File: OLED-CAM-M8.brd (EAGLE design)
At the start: 87.6 x 61 mm, 16 parts, among them J5 U.FL

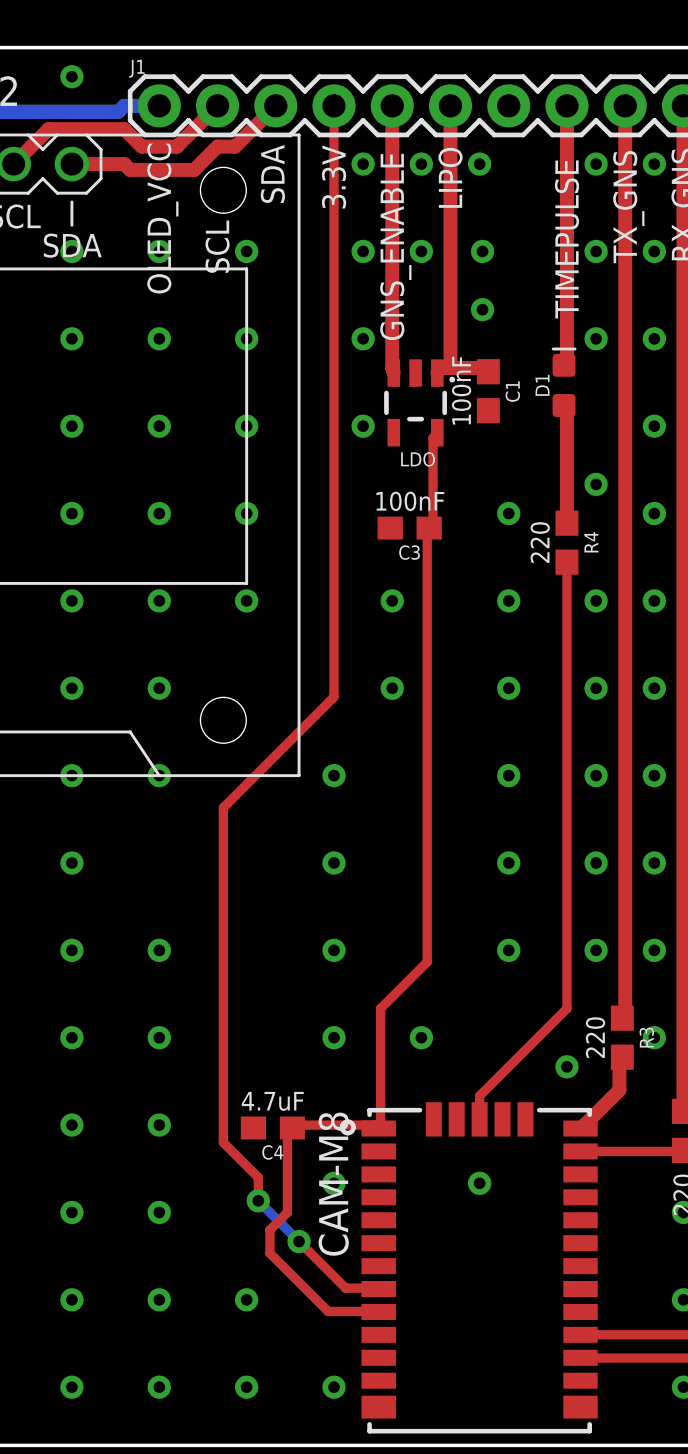
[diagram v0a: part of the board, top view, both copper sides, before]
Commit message: Moved 3v rail
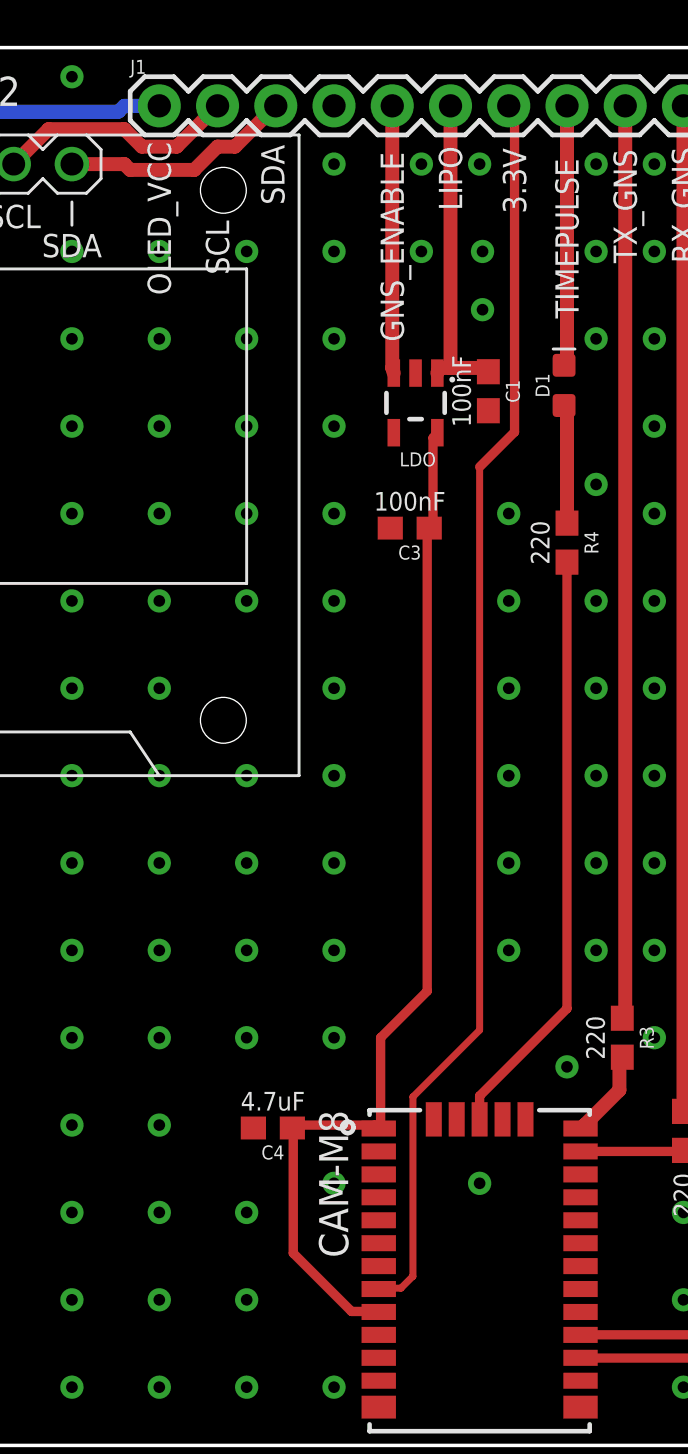
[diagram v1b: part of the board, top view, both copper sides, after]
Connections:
- net 3.3V: now also J1.7; no longer J1.4
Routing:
- net 3.3V: track 57.2 -> 54.7 mm, vias 2 -> 0
- net GNS_VCC: track 47.3 -> 45.6 mm
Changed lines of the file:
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@@
 Only one ANT jumper
 should be bridged</text>
-<wire x1="42.037" y1="14.859" x2="42.037" y2="13.589" width="0.0508" layer="41"/>
 <text x="58.928" y="54.102" size="1.016" layer="25" font="vector" ratio="20" rot="R90">GND</text>
 <text x="56.388" y="52.451" size="1.016" layer="25" font="vector" ratio="20" rot="R90">SPARE</text>
@@
 <text x="43.688" y="53.848" size="1.016" layer="25" font="vector" ratio="20" rot="R90">LIPO</text>
 <text x="41.148" y="48.133" size="1.016" layer="25" font="vector" ratio="20" rot="R90">GNS_ENABLE</text>
-<text x="38.608" y="53.848" size="1.016" layer="25" font="vector" ratio="20" rot="R90">3.3V</text>
+<text x="46.482" y="53.721" size="1.016" layer="25" font="vector" ratio="20" rot="R90">3.3V</text>
 <text x="35.941" y="54.102" size="1.016" layer="25" font="vector" ratio="20" rot="R90">SDA</text>
 <text x="30.988" y="50.165" size="1.016" layer="25" font="vector" ratio="20" rot="R90">OLED_VCC</text>
@@
 <clearance class="1" value="0.4064"/>
 </class>
-<class number="2" name="gns" width="0.4064" drill="0">
-<clearance class="2" value="0.4064"/>
+<class number="2" name="gns" width="0.3048" drill="0">
+<clearance class="2" value="0.3048"/>
 </class>
 </classes>
@@
 <via x="44.577" y="52.07" extent="1-16" drill="0.508"/>
 <via x="41.91" y="52.07" extent="1-16" drill="0.508"/>
-<via x="39.37" y="48.26" extent="1-16" drill="0.508"/>
-<via x="39.37" y="52.07" extent="1-16" drill="0.508"/>
-<via x="39.37" y="44.45" extent="1-16" drill="0.508"/>
-<via x="39.37" y="55.88" extent="1-16" drill="0.508"/>
 <via x="57.15" y="40.64" extent="1-16" drill="0.508"/>
 <via x="57.15" y="44.45" extent="1-16" drill="0.508"/>
@@
 <via x="64.77" y="13.97" extent="1-16" drill="0.508"/>
 <via x="38.1" y="17.78" extent="1-16" drill="0.508"/>
-<via x="41.91" y="17.78" extent="1-16" drill="0.508"/>
-<via x="40.64" y="33.02" extent="1-16" drill="0.508"/>
-<via x="40.64" y="36.83" extent="1-16" drill="0.508"/>
 <via x="45.72" y="40.64" extent="1-16" drill="0.508"/>
+<via x="34.29" y="17.78" extent="1-16" drill="0.508"/>
+<via x="34.29" y="10.16" extent="1-16" drill="0.508"/>
+<via x="34.29" y="21.59" extent="1-16" drill="0.508"/>
+<via x="34.29" y="25.4" extent="1-16" drill="0.508"/>
+<via x="30.48" y="25.4" extent="1-16" drill="0.508"/>
+<via x="34.29" y="29.21" extent="1-16" drill="0.508"/>
+<via x="38.1" y="33.02" extent="1-16" drill="0.508"/>
+<via x="38.1" y="36.83" extent="1-16" drill="0.508"/>
+<via x="38.1" y="40.64" extent="1-16" drill="0.508"/>
+<via x="38.1" y="44.45" extent="1-16" drill="0.508"/>
+<via x="38.1" y="48.26" extent="1-16" drill="0.508"/>
+<via x="38.1" y="52.07" extent="1-16" drill="0.508"/>
+<via x="38.1" y="55.88" extent="1-16" drill="0.508"/>
 </signal>
 <signal name="3.3V" class="2">
 <contactref element="U$5" pad="8"/>
-<contactref element="J1" pad="4"/>
-<wire x1="38.608" y1="6.858" x2="39.878" y2="6.858" width="0.4064" layer="1"/>
-<wire x1="36.576" y1="8.89" x2="38.608" y2="6.858" width="0.4064" layer="1"/>
-<wire x1="34.798" y1="10.668" x2="36.576" y2="8.89" width="0.4064" layer="16"/>
-<wire x1="34.798" y1="11.684" x2="34.798" y2="10.668" width="0.4064" layer="1"/>
-<wire x1="33.274" y1="13.208" x2="34.798" y2="11.684" width="0.4064" layer="1"/>
-<wire x1="33.274" y1="27.813" x2="33.274" y2="13.208" width="0.4064" layer="1"/>
-<wire x1="38.1" y1="32.639" x2="33.274" y2="27.813" width="0.4064" layer="1"/>
-<wire x1="38.1" y1="58.42" x2="38.1" y2="32.639" width="0.4064" layer="1"/>
-<wire x1="39.878" y1="6.858" x2="40.05" y2="6.82" width="0.4064" layer="1"/>
-<via x="36.576" y="8.89" extent="1-16" drill="0.508"/>
-<via x="34.798" y="10.668" extent="1-16" drill="0.508"/>
+<contactref element="J1" pad="7"/>
+<wire x1="45.974" y1="44.196" x2="44.45" y2="42.672" width="0.4064" layer="1"/>
+<wire x1="45.974" y1="58.166" x2="45.974" y2="44.196" width="0.4064" layer="1"/>
+<wire x1="45.72" y1="58.42" x2="45.974" y2="58.166" width="0.4064" layer="1"/>
+<wire x1="44.45" y1="18.1102625" x2="44.45" y2="42.672" width="0.3048" layer="1"/>
+<wire x1="44.45" y1="18.1102625" x2="41.5412" y2="15.2014625" width="0.3048" layer="1"/>
+<wire x1="41.5412" y1="7.366" x2="41.5412" y2="15.2014625" width="0.3048" layer="1"/>
+<wire x1="41.021" y1="6.858" x2="40.132" y2="6.858" width="0.3048" layer="1"/>
+<wire x1="41.529" y1="7.366" x2="41.021" y2="6.858" width="0.3048" layer="1"/>
+<wire x1="41.529" y1="7.366" x2="41.5412" y2="7.366" width="0.3048" layer="1"/>
+<wire x1="40.132" y1="6.858" x2="40.05" y2="6.82" width="0.3048" layer="1"/>
 </signal>
 <signal name="TX_GNS">
@@
 <contactref element="U$5" pad="9"/>
 <contactref element="U$5" pad="1"/>
-<wire x1="42.164" y1="40.005" x2="42.252" y2="40.005" width="0.4064" layer="1"/>
-<wire x1="42.418" y1="40.005" x2="42.252" y2="40.005" width="0.4064" layer="1"/>
-<wire x1="37.846" y1="5.842" x2="39.878" y2="5.842" width="0.4064" layer="1"/>
-<wire x1="35.306" y1="8.382" x2="37.846" y2="5.842" width="0.4064" layer="1"/>
-<wire x1="35.306" y1="9.398" x2="35.306" y2="8.382" width="0.4064" layer="1"/>
-<wire x1="36.068" y1="10.16" x2="35.306" y2="9.398" width="0.4064" layer="1"/>
-<wire x1="36.068" y1="13.716" x2="36.068" y2="10.16" width="0.4064" layer="1"/>
-<wire x1="39.878" y1="5.842" x2="40.05" y2="5.82" width="0.4064" layer="1"/>
-<wire x1="36.068" y1="13.716" x2="36.283" y2="13.843" width="0.4064" layer="1"/>
 <wire x1="36.322" y1="13.97" x2="39.878" y2="13.97" width="0.4064" layer="1"/>
 <wire x1="39.878" y1="13.97" x2="40.05" y2="13.82" width="0.4064" layer="1"/>
 <wire x1="36.322" y1="13.97" x2="36.283" y2="13.843" width="0.4064" layer="1"/>
 <wire x1="42.418" y1="43.942" x2="42.418" y2="40.132" width="0.4064" layer="1"/>
-<wire x1="42.418" y1="40.132" x2="42.252" y2="40.005" width="0.4064" layer="1"/>
 <wire x1="42.418" y1="43.942" x2="42.606" y2="44.1659" width="0.4064" layer="1"/>
-<wire x1="42.164" y1="21.082" x2="42.164" y2="39.878" width="0.4064" layer="1"/>
-<wire x1="40.132" y1="19.05" x2="42.164" y2="21.082" width="0.4064" layer="1"/>
-<wire x1="40.132" y1="13.97" x2="40.132" y2="19.05" width="0.4064" layer="1"/>
-<wire x1="42.164" y1="39.878" x2="42.252" y2="40.005" width="0.4064" layer="1"/>
+<wire x1="38.862" y1="5.842" x2="39.878" y2="5.842" width="0.4064" layer="1"/>
+<wire x1="36.322" y1="8.382" x2="38.862" y2="5.842" width="0.4064" layer="1"/>
+<wire x1="36.322" y1="13.716" x2="36.322" y2="8.382" width="0.4064" layer="1"/>
+<wire x1="39.878" y1="5.842" x2="40.05" y2="5.82" width="0.4064" layer="1"/>
+<wire x1="42.164" y1="19.812" x2="42.164" y2="39.878" width="0.4064" layer="1"/>
+<wire x1="40.132" y1="17.78" x2="42.164" y2="19.812" width="0.4064" layer="1"/>
+<wire x1="40.132" y1="13.97" x2="40.132" y2="17.78" width="0.4064" layer="1"/>
 <wire x1="40.132" y1="13.97" x2="40.05" y2="13.82" width="0.4064" layer="1"/>
+<wire x1="42.418" y1="40.132" x2="42.252" y2="40.005" width="0.3048" layer="1"/>
+<wire x1="42.164" y1="39.878" x2="42.252" y2="40.005" width="0.3048" layer="1"/>
+<wire x1="36.322" y1="13.716" x2="36.283" y2="13.843" width="0.3048" layer="1"/>
 </signal>
 <signal name="GNS_ENABLE">

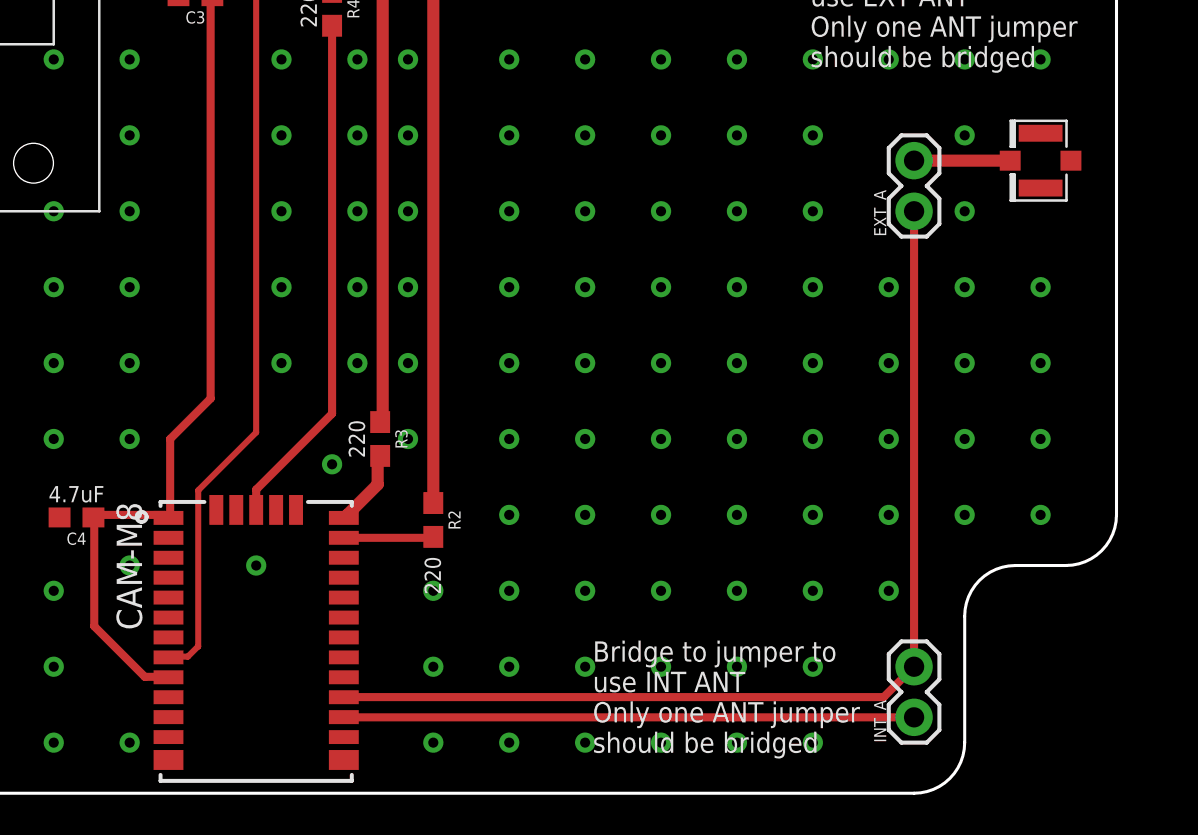
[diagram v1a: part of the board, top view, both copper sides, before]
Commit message: removed ufl and jumpers
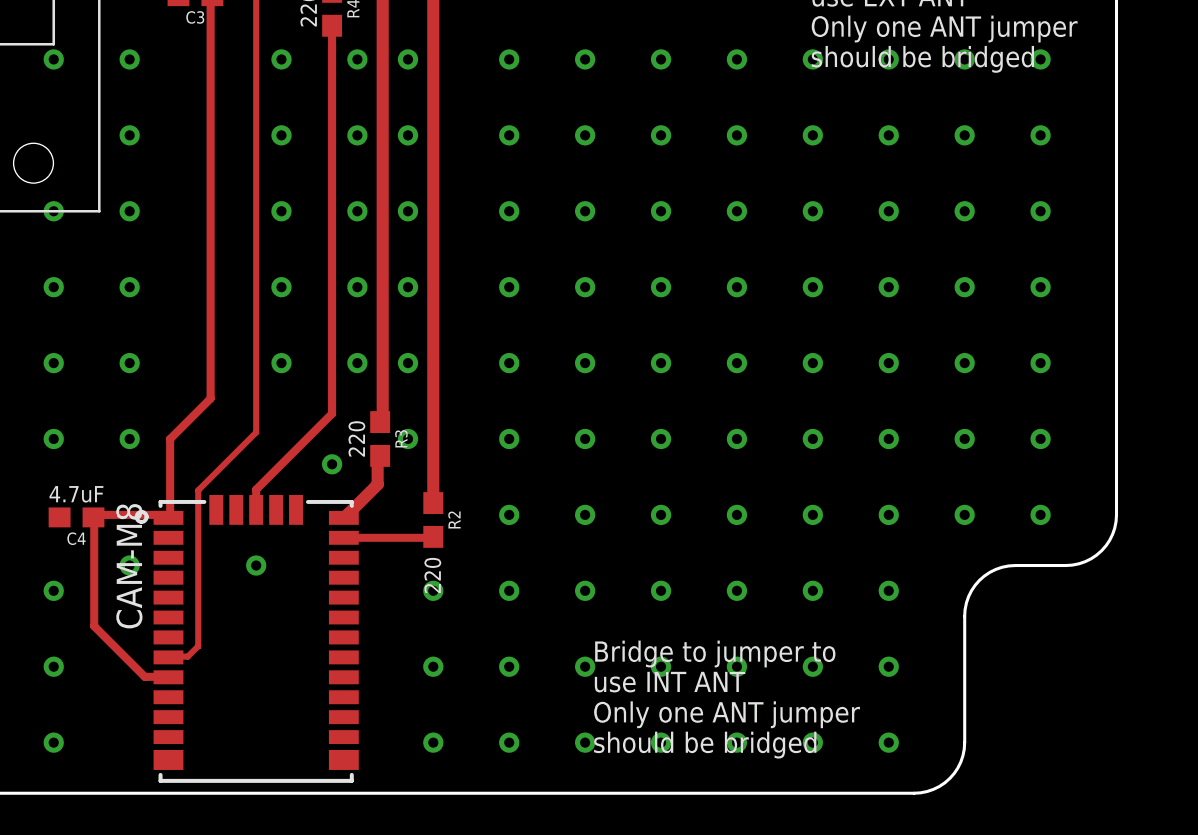
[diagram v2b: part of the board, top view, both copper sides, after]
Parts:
- removed EXT_A, INT_A: (no value), SparkFun-Connectors:1X02
- removed J5: U.FL, SparkFun-Connectors:U.FL
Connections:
- removed net N$6: EXT_A.2, J5.FEED
- removed net N$7: INT_A.1, U$5.16
- net GND: no longer J5.1, J5.2
- net N$5: now also U$5.16; no longer EXT_A.1, INT_A.2
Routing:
- net N$5: track 52.1 -> 0.00 mm
- net N$7: track 28.6 -> 0.00 mm
- net N$6: track 4.83 -> 0.00 mm
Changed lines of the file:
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@@
 <attribute name="VALUE" x="48.768" y="46.228" size="0.6096" layer="27" font="vector" ratio="20" rot="R90" align="top-center"/>
-</element>
-<element name="J5" library="SparkFun-Connectors" library_urn="urn:adsk.eagle:library:513" package="U.FL" package3d_urn="urn:adsk.eagle:package:38237/1" value="U.FL" x="83.82" y="31.75" smashed="yes" rot="R180">
-<attribute name="PROD_ID" value="CONN-09193" x="83.82" y="31.75" size="1.778" layer="27" rot="R180" display="off"/>
-<attribute name="SF_ID" value="WRL-09144" x="83.82" y="31.75" size="1.778" layer="27" rot="R180" display="off"/>
-<attribute name="VALUE" x="83.82" y="34.29" size="0.6096" layer="27" font="vector" ratio="20" rot="R180" align="top-left"/>
-</element>
-<element name="INT_A" library="SparkFun-Connectors" library_urn="urn:adsk.eagle:library:513" package="1X02" package3d_urn="urn:adsk.eagle:package:38039/1" value="" x="77.47" y="3.81" smashed="yes" rot="R90">
-<attribute name="NAME" x="76.073" y="2.54" size="0.6096" layer="25" font="vector" ratio="20" rot="R90"/>
-<attribute name="VALUE" x="79.502" y="2.54" size="0.6096" layer="27" font="vector" ratio="20" rot="R90"/>
-</element>
-<element name="EXT_A" library="SparkFun-Connectors" library_urn="urn:adsk.eagle:library:513" package="1X02" package3d_urn="urn:adsk.eagle:package:38039/1" value="" x="77.47" y="29.21" smashed="yes" rot="R90">
-<attribute name="NAME" x="76.073" y="27.94" size="0.6096" layer="25" font="vector" ratio="20" rot="R90"/>
-<attribute name="VALUE" x="79.502" y="27.94" size="0.6096" layer="27" font="vector" ratio="20" rot="R90"/>
 </element>
 <element name="U$2" library="diy-modules" package="DISPLAY-OLED-128X64-I2C" value="DISPLAY-OLED-128X64-I2C" x="22.86" y="43.18" smashed="yes">
@@
 <vertex x="8.89" y="58.42" curve="-90"/>
 </polygon>
-<contactref element="J5" pad="2"/>
-<contactref element="J5" pad="1"/>
 <contactref element="J1" pad="12"/>
 <via x="38.1" y="11.43" extent="1-16" drill="0.508"/>
@@
 <via x="30.48" y="2.54" extent="1-16" drill="0.508"/>
 <via x="34.29" y="6.35" extent="1-16" drill="0.508"/>
-<via x="38.1" y="2.54" extent="1-16" drill="0.508"/>
 <via x="34.29" y="2.54" extent="1-16" drill="0.508"/>
 <via x="38.1" y="29.21" extent="1-16" drill="0.508"/>
@@
 <via x="38.1" y="52.07" extent="1-16" drill="0.508"/>
 <via x="38.1" y="55.88" extent="1-16" drill="0.508"/>
+<via x="76.2" y="6.35" extent="1-16" drill="0.508"/>
+<via x="76.2" y="2.54" extent="1-16" drill="0.508"/>
+<via x="76.2" y="29.21" extent="1-16" drill="0.508"/>
+<via x="76.2" y="33.02" extent="1-16" drill="0.508"/>
+<via x="83.82" y="33.02" extent="1-16" drill="0.508"/>
+<via x="83.82" y="29.21" extent="1-16" drill="0.508"/>
 </signal>
 <signal name="3.3V" class="2">
@@
 <wire x1="43.18" y1="58.42" x2="43.18" y2="46.99" width="0.6096" layer="1"/>
 </signal>
-<signal name="N$6">
-<contactref element="J5" pad="FEED"/>
-<contactref element="EXT_A" pad="2"/>
-<wire x1="77.47" y1="31.75" x2="82.295" y2="31.75" width="0.6096" layer="1"/>
-</signal>
-<signal name="N$5" class="2">
-<contactref element="EXT_A" pad="1"/>
-<contactref element="U$5" pad="17"/>
-<contactref element="INT_A" pad="2"/>
-<wire x1="75.946" y1="4.826" x2="49.022" y2="4.826" width="0.4064" layer="1"/>
-<wire x1="77.47" y1="6.35" x2="75.946" y2="4.826" width="0.4064" layer="1"/>
-<wire x1="49.022" y1="4.826" x2="48.85" y2="4.82" width="0.4064" layer="1"/>
-<wire x1="77.47" y1="6.35" x2="77.47" y2="29.21" width="0.4064" layer="1"/>
-</signal>
-<signal name="N$7" class="2">
-<contactref element="U$5" pad="16"/>
-<contactref element="INT_A" pad="1"/>
-<wire x1="77.47" y1="3.81" x2="49.022" y2="3.81" width="0.4064" layer="1"/>
-<wire x1="49.022" y1="3.81" x2="48.85" y2="3.82" width="0.4064" layer="1"/>
-</signal>
 <signal name="TIMEPULSE">
 <contactref element="D1" pad="C"/>
@@
 <wire x1="35.56" y1="58.42" x2="33.782" y2="56.642" width="0.6096" layer="1"/>
 </signal>
+<signal name="N$5">
+<contactref element="U$5" pad="16"/>
+<contactref element="U$5" pad="17"/>
+<wire x1="48.85" y1="4.82" x2="48.85" y2="3.82" width="0" layer="19" extent="1-1"/>
+</signal>
 </signals>
